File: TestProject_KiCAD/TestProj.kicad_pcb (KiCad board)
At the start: 2 copper layers, 72 parts, among them J1 USB4105-GF-A-120, J2 Conn_02x03_Odd_Even, J3 TF-Push, Q1 BC817, Q2 BC817, Q3 IRLML6401, Q4 BC817, Q5 BC817, Q6 BC817, Q7 2N7002P, Q8 2N7002P, Q9 BC817, U1 AP2125N-3.0TRG1, U2 STM32F411VET6, U3 AP2125N-3.0TRG1, U4 AP2125N-3.0TRG1, Y1 ECS-2520MV-080-CN-TR, Y2 ECS-327MVATX-3-CN-TR

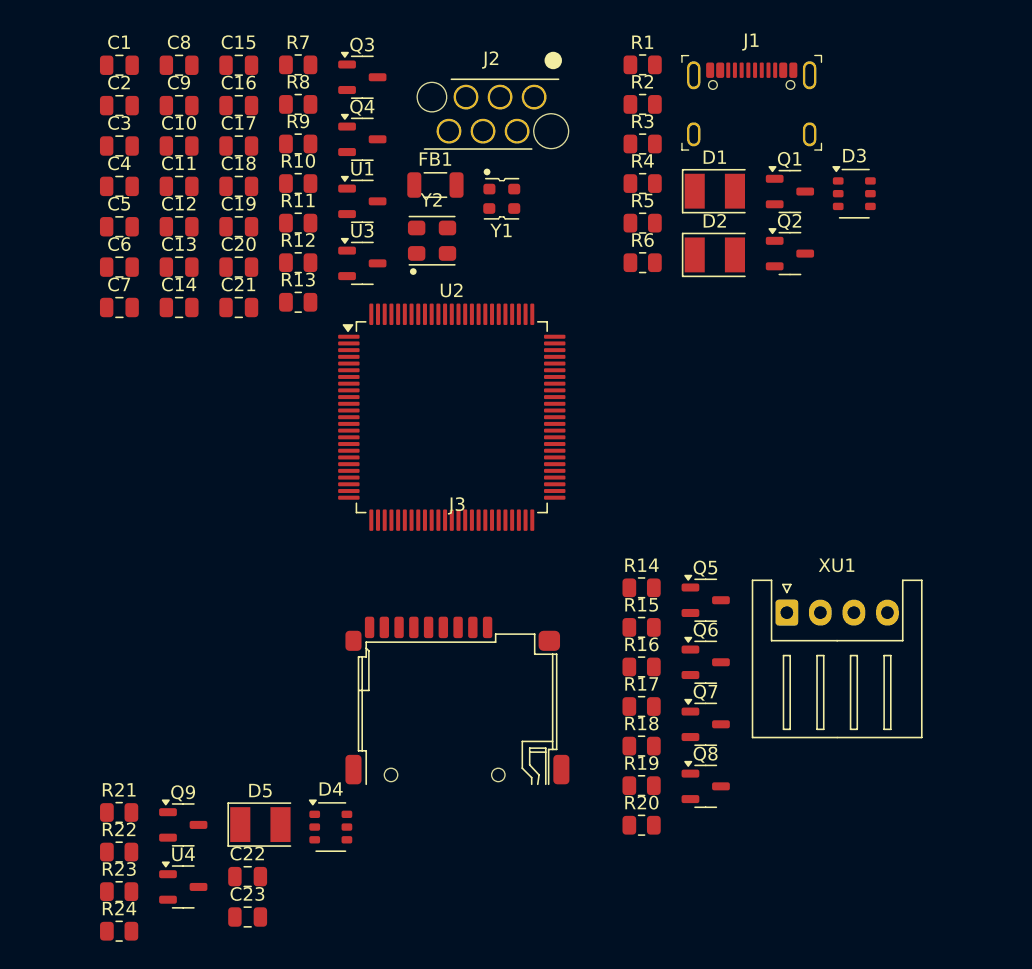
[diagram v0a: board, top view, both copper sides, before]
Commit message: added Multi-Unit supoort: - python code parses symbol geometry in units (keys: Unit1, Unit2, ...) - JS draws a gui on the symbol konva stage to select the unit
refactored JS-Code a bit again (geometry is placed like it is on the layer, instead of shifting it by stage.width()/2 and .height()/2. Also needed to invert the y-axis, at it is mirrored on Konva compared to KiCAD.

added a settings page, to toggle footprint layers and set the color, pretty barebone for now, as it was just a quick test
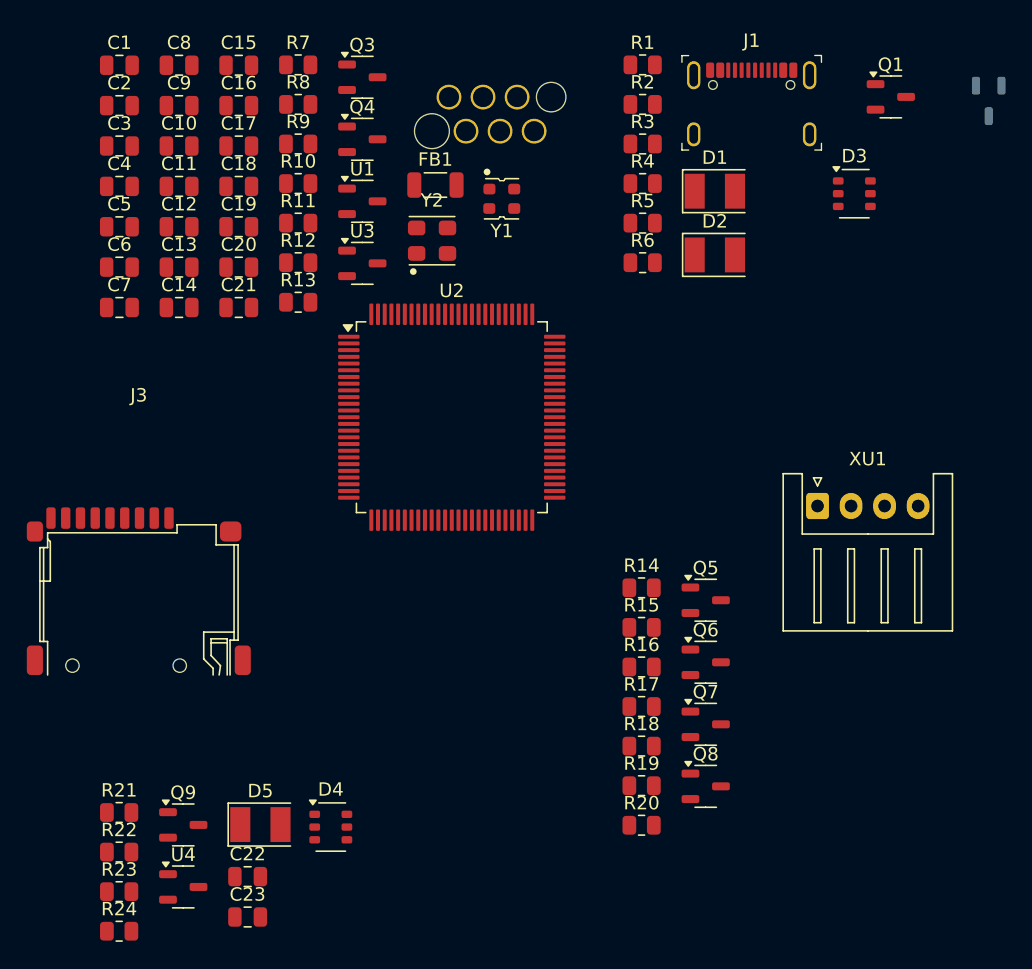
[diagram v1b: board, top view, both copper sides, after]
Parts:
- J2, Q2: moved to B.Cu
- moved J3 25.1 mm to (83.2, 123.9)
- moved Q2 18.7 mm to (146.6, 81.8), turned to -90 degrees
- moved Q1 10.3 mm to (139.3, 81.5)
- moved XU1 8.27 mm to (133.8, 112.0)
- turned J2 to 180 degrees
